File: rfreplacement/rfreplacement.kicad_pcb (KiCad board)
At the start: 2 copper layers, 43.9 x 55.9 mm, 27 parts

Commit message: Pinheaders moved to the bottom side.
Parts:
- GND1, GND2, GND3: moved to B.Cu
- moved GND1 2.54 mm to (144.8, 84.3)
- turned GND2 to 270 degrees
- turned GND3 to 270 degrees

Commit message: Layout cleanup.
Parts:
- moved REG2 20.9 mm to (119.4, 101.6), turned to 0 degrees
- moved C1 20.3 mm to (112.8, 102.9), turned to 270 degrees
- moved JPLUM1 5.48 mm to (117.6, 95.0)
- moved R30 5.48 mm to (114.4, 70.2)
- moved R32 5.48 mm to (114.4, 75.7)
- moved R38 5.48 mm to (121.4, 90.6)
- moved R39 5.48 mm to (114.4, 85.5)
- moved C9 5.48 mm to (123.4, 73.2)
- moved R33 5.48 mm to (116.7, 60.7)
- moved R34 5.48 mm to (116.7, 65.8)
- moved R36 5.48 mm to (122.4, 95.0)
- moved R37 5.48 mm to (122.4, 85.5)
- moved R40 5.48 mm to (117.0, 85.5)
- moved R35 5.48 mm to (116.7, 63.2)
- moved AMP2 5.48 mm to (119.5, 73.4)
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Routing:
- net +12V: track 37.0 -> 8.81 mm
- net /LUMA_OUT: track 48.8 -> 37.2 mm, vias 0 -> 1
- net GNDA: track 22.0 -> 14.3 mm
- net /CHROMA_IN: track 7.26 -> 12.2 mm
- net /LUMA_IN: track 14.5 -> 18.1 mm
- net /COMPOSITE_OUT: track 6.48 -> 9.96 mm
- net /CHROMA_OUT: track 36.4 -> 38.5 mm
- net Net-(AMP2-Pad8): track 16.2 -> 15.6 mm

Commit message: PCB labels cleanup.
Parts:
- moved C1 6.32 mm to (117.6, 106.9), turned to 180 degrees
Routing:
- net GNDA: track 14.3 -> 33.3 mm
- net +12V: track 8.81 -> 12.0 mm
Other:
- board text added: "C64 Video Enhancement, Analog Only github.com/c0pperdragon PCB design for ASSY NO.250469 by Pawel Mandes / devzine.pl github.com/pmandes/C64-RF-Modulator"
- board text added: "RF MODULATOR REPLACEMENT V1.0 FOR ASSY NO.250469"
- board text removed: "C64 Video Enhancement, Analog Only github.com/c0pperdragon"
- board text removed: "FOR ASSY NO.250469"
- board text removed: "PCB DESIGN by Pawel Mandes / devzine.pl"

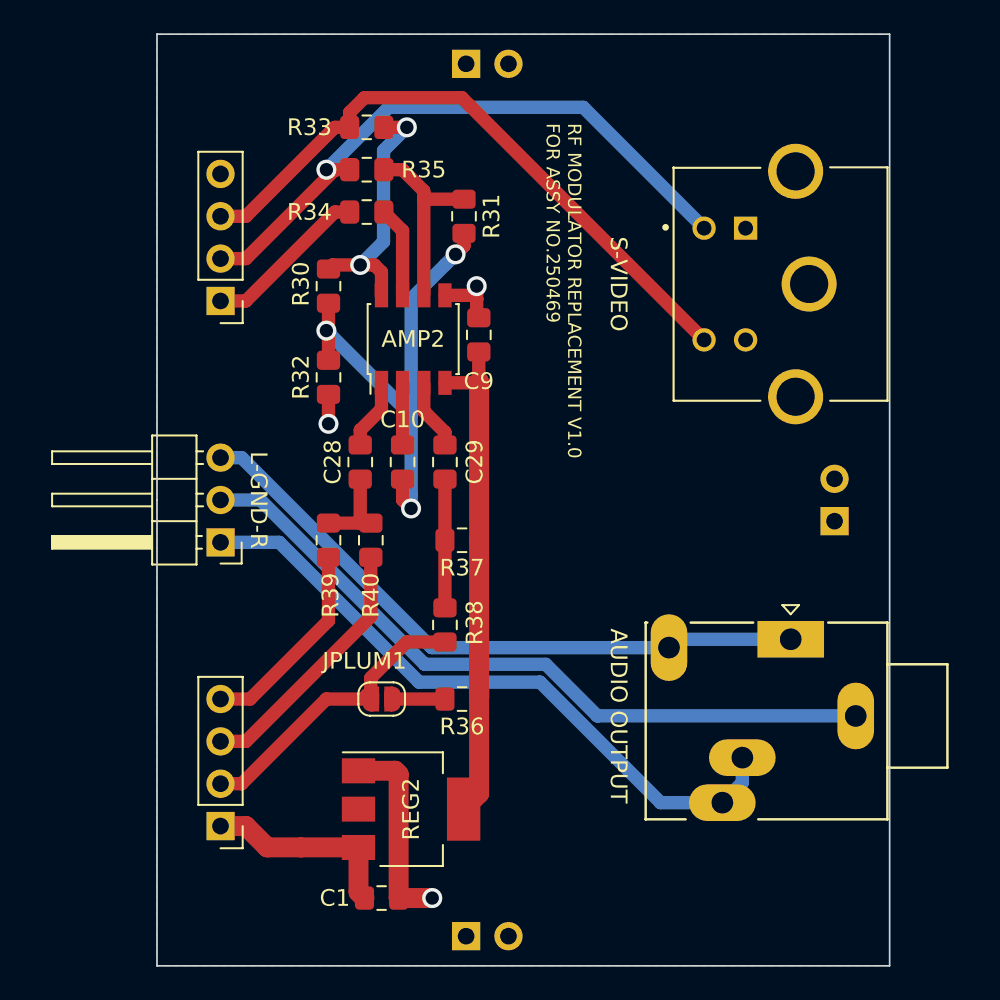
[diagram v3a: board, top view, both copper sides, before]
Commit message: Dimensions adjusted.
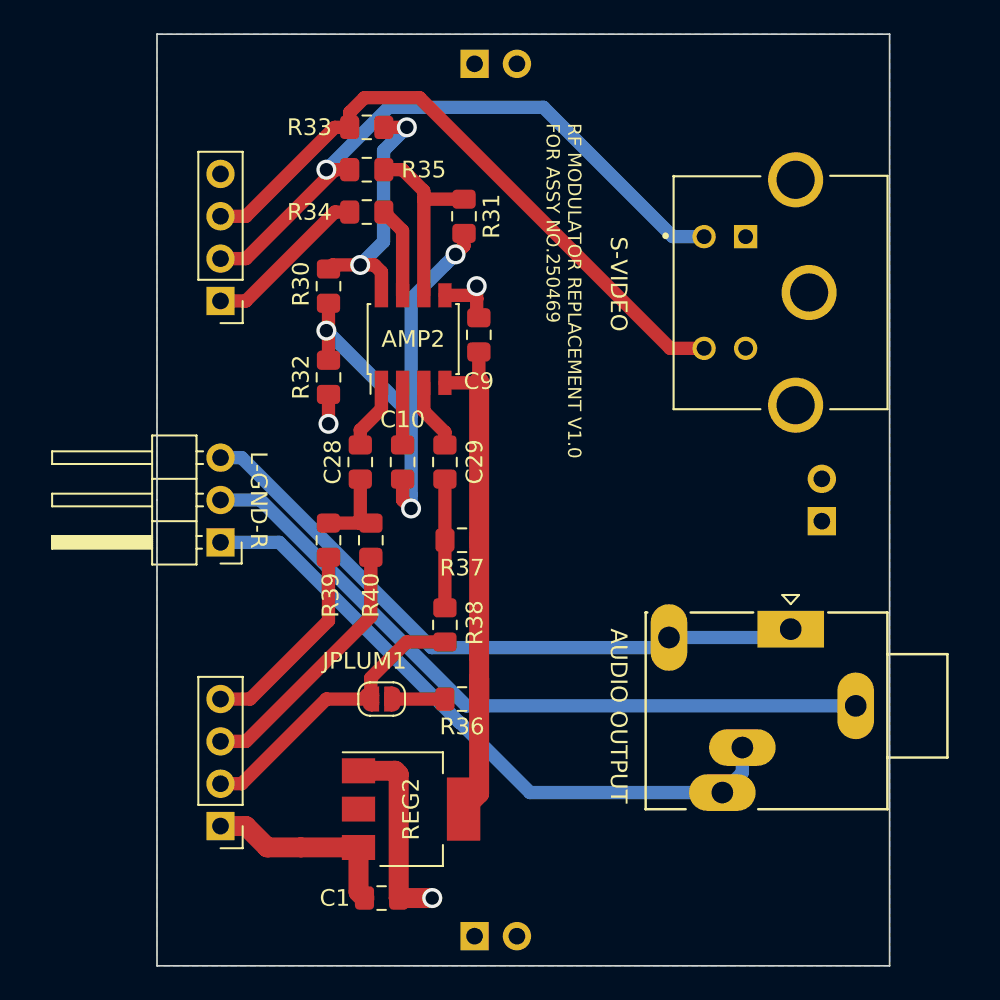
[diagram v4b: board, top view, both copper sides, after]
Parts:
- moved GND1 0.76 mm to (144.0, 84.3)
- moved STEREO_OUT1 0.61 mm to (142.2, 90.8)
- moved GND2 0.51 mm to (123.2, 109.2)
- moved GND3 0.51 mm to (123.2, 56.9)
- moved S-VIDEO1 0.51 mm to (139.4, 70.6)
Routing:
- net /AUDIO_RIGHT: track 39.8 -> 41.2 mm
- net /AUDIO_LEFT: track 39.1 -> 40.1 mm

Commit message: Connectors position adjusted.
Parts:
- moved GND1 1.02 mm to (145.0, 84.3)
- moved STEREO_OUT1 0.66 mm to (142.0, 91.4)
- moved S-VIDEO1 0.51 mm to (139.4, 70.1)
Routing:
- net /LUMA_IN: track 18.1 -> 15.8 mm
- net /AUDIO_RIGHT: track 41.2 -> 39.6 mm
- net /AUDIO_LEFT: track 40.1 -> 41.2 mm

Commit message: New gerber files.
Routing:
- net /LUMA_IN: track 15.8 -> 18.1 mm
- net /AUDIO_GND: track 43.6 -> 44.5 mm

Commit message: PCB ver 1.2
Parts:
- added FB1: Ferrite Bead, Inductor_SMD:L_0805_2012Metric_Pad1.15x1.40mm_HandSolder, F.Cu at (115.1, 78.7)
- added FB2: Ferrite Bead, Inductor_SMD:L_0805_2012Metric_Pad1.15x1.40mm_HandSolder, F.Cu at (108.5, 78.7)
- added FB3: Alternative THT, Resistor_THT:R_Axial_DIN0207_L6.3mm_D2.5mm_P7.62mm_Horizontal, B.Cu at (115.1, 74.2)
- added FB4: Alternative THT, Resistor_THT:R_Axial_DIN0207_L6.3mm_D2.5mm_P7.62mm_Horizontal, B.Cu at (108.4, 74.2)
- added J1: Conn_01x02, Connector_PinHeader_2.00mm:PinHeader_1x02_P2.00mm_Vertical, F.Cu at (146.2, 63.8)
- added J2: Conn_01x02, Connector_PinHeader_2.00mm:PinHeader_1x02_P2.00mm_Vertical, F.Cu at (148.2, 63.8)
- added J3: Conn_01x02, Connector_PinHeader_2.00mm:PinHeader_1x02_P2.00mm_Vertical, F.Cu at (150.2, 63.8)
- added REF**: OSHW-Logo2_9.8x8mm_SilkScreen, Symbol:OSHW-Logo2_9.8x8mm_SilkScreen, B.Cu at (106.2, 91.4)
- added REF**: KiCad-Logo2_5mm_SilkScreen, Symbol:KiCad-Logo2_5mm_SilkScreen, B.Cu at (141.2, 80.5)
- C1, C10, C28, C29, C9: footprint Capacitor_SMD:C_0805_2012Metric_Pad1.15x1.40mm_HandSolder -> Capacitor_SMD:C_0805_2012Metric_Pad1.18x1.45mm_HandSolder
- R30, R31, R32, R33, R34, R35, R36, R37, R38, R39, R40: footprint Resistor_SMD:R_0805_2012Metric_Pad1.15x1.40mm_HandSolder -> Resistor_SMD:R_0805_2012Metric_Pad1.20x1.40mm_HandSolder
- moved GND2 37.1 mm to (150.9, 84.6), turned to 0 degrees
- moved GND3 37.1 mm to (98.6, 84.6), turned to 0 degrees
- moved RFCONC2 36.4 mm to (144.3, 99.8), turned to -90 degrees
- moved C1 35.2 mm to (148.6, 90.2), turned to -90 degrees
- moved R33 33.6 mm to (102.4, 91.0), turned to 90 degrees
- moved R35 30.2 mm to (104.9, 91.0), turned to 90 degrees
- moved RFCONC1 29.1 mm to (112.8, 99.8), turned to -90 degrees
- moved GND1 28.8 mm to (126.0, 62.7), turned to 90 degrees
- moved S-VIDEO1 27.7 mm to (111.8, 68.3), turned to 0 degrees
- moved LM1117-3.3 27.3 mm to (143.3, 88.4), turned to 90 degrees
- moved STEREO_OUT1 27.2 mm to (133.1, 65.8), turned to -90 degrees
- moved R34 26.9 mm to (107.4, 91.0), turned to -90 degrees
- moved R31 24.3 mm to (107.7, 85.2), turned to 0 degrees
- moved AUDIO_OUT1 24.0 mm to (127.3, 99.8), turned to -90 degrees
- moved R30 23.3 mm to (111.9, 93.3), turned to 180 degrees
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- renumbered REG2 to LM1117-3.3, AMP2 to THS3716
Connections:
- net +12V renamed +5V
- LM1117-3.3 pad 2: (no net) -> unconnected-(REG2-Pad2)
- RFCONC1 pad 4: (no net) -> /AUDIO_OUT
- S-VIDEO1 pad 3: /LUMA_OUT -> Net-(FB2-Pad2)
- S-VIDEO1 pad 4: /CHROMA_OUT -> Net-(FB1-Pad2)
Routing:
- net /AUDIO_OUT: track 0.00 -> 87.4 mm
- net /AUDIO_RIGHT: track 39.7 -> 57.1 mm
- net /LUMA_OUT: track 37.2 -> 50.0 mm, vias 1 -> 0
- net /AUDIO_LEFT: track 41.2 -> 52.2 mm
- net /AUDIO_GND: track 44.5 -> 55.1 mm
- net Net-(FB1-Pad2): track 0.00 -> 6.86 mm
- net Net-(FB2-Pad2): track 0.00 -> 6.84 mm
- net /CHROMA_OUT: track 38.5 -> 44.0 mm
- net GNDA: track 33.3 -> 31.2 mm, vias 3 -> 21
- net /3V3X: track 31.2 -> 29.9 mm
- added copper zone on F.Cu, net GNDA
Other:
- board size 43.9 x 55.9 mm -> 55.9 x 43.9 mm
- net class Default removed
- net class power removed
- board text added: "+5V"
- board text added: "."
- board text added: "1"
- board text added: "4"
- board text added: "5"
- board text added: "8"
- board text added: "AUD"
- board text added: "C64 Video Enhancement, Analog Only github.com/c0pperdragon PCB design for ASSY NO.250469 / Ver 1.2 by Pawel Mandes / devzine.pl github.com/pmandes/C64-RF-Modulator"
- board text added: "CHR"
- board text added: "CHROMINANCE"
- board text added: "CIN"
- board text added: "CMP"
- board text added: "GND"
- board text added: "INTERNAL AUDIO"
- board text added: "LEFT"
- board text added: "LIN"
- board text added: "LUM"
- board text added: "LUMINANCE"
- board text added: "RF MODULATOR REPLACEMENT FOR ASSY NO.250469 / VER 1.2"
- board text added: "RIGHT"
- board text removed: "C64 Video Enhancement, Analog Only github.com/c0pperdragon PCB design for ASSY NO.250469 by Pawel Mandes / devzine.pl github.com/pmandes/C64-RF-Modulator"
- board text removed: "RF MODULATOR REPLACEMENT V1.0 FOR ASSY NO.250469"
